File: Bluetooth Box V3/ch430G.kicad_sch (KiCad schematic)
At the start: 6 parts, among them U4 AMS1117-1.8, U8 AZ1117-3.3

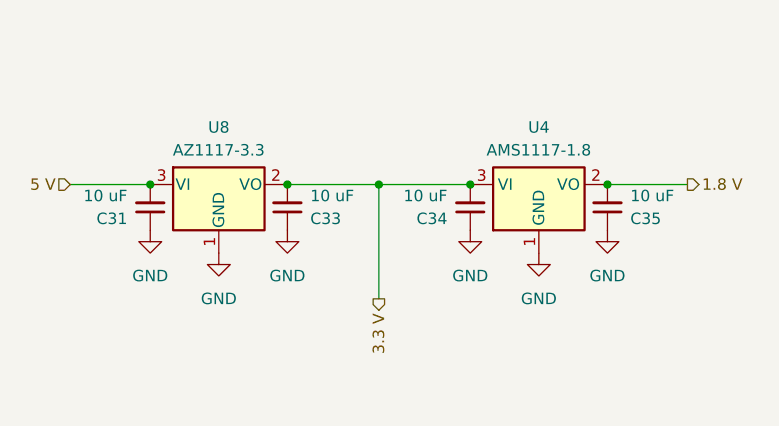
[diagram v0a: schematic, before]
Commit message: ESP32 Wechsel angefangen
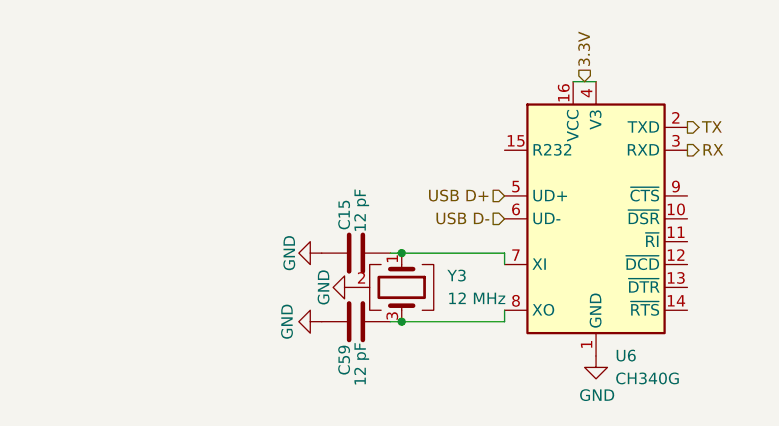
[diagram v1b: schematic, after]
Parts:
- removed C31, C33, C34, C35: 10 uF, Capacitor_SMD:C_0805_2012Metric, symbol Device:C_Small
- removed U4: AMS1117-1.8, Package_TO_SOT_SMD:SOT-223-3_TabPin2, symbol Regulator_Linear:AMS1117-1.8
- removed U8: AZ1117-3.3, Package_TO_SOT_SMD:TO-252-2, symbol Regulator_Linear:AZ1117-3.3
- added C15, C59: 12 pF, Capacitor_SMD:C_0805_2012Metric, symbol Device:C
- added U6: CH340G, Package_SO:SOIC-16_3.9x9.9mm_P1.27mm, symbol Interface_USB:CH340G
- added Y3: 12 MHz, Crystal:Crystal_SMD_3225-4Pin_3.2x2.5mm, symbol Device:Crystal_GND24
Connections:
- net GND: now also C15.1, C59.1, U6.1 (GND), Y3.2 (G), Y3.4 (G)
- new net: C15.2, U6.7 (XI), Y3.1
- new net: C59.2, U6.8 (XO), Y3.3
- new net 3.3V: U6.16 (VCC), U6.4 (V3)
- new net RX: U6.3 (RXD)
- new net TX: U6.2 (TXD)
- new net USB D+: U6.5 (UD+)
- new net USB D-: U6.6 (UD-)

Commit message: Idiotencheck #1
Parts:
- added C79: 100 nF, Capacitor_SMD:C_0805_2012Metric, symbol Device:C
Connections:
- net 3.3V: now also C79.2
- net GND: now also C79.1
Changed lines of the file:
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@@
 		(color 0 0 0 0)
 	)
+	(junction
+		(at 115.57 66.04)
+		(diameter 0)
+		(color 0 0 0 0)
+	)
+	(junction
+		(at 115.57 62.23)
+		(diameter 0)
+		(color 0 0 0 0)
+	)
+	(wire
+		(pts
+			(xy 115.57 66.04) (xy 116.84 66.04)
+		)
+		(stroke
+			(width 0)
+			(type default)
+		)
+	)
+	(wire
+		(pts
+			(xy 115.57 57.15) (xy 115.57 62.23)
+		)
+		(stroke
+			(width 0)
+			(type default)
+		)
+	)
 	(wire
 		(pts
@@
 	(wire
 		(pts
-			(xy 114.3 66.04) (xy 116.84 66.04)
+			(xy 114.3 66.04) (xy 115.57 66.04)
+		)
+		(stroke
+			(width 0)
+			(type default)
+		)
+	)
+	(wire
+		(pts
+			(xy 115.57 66.04) (xy 115.57 62.23)
 		)
 		(stroke
@@
 			(width 0)
 			(type default)
-		)
-	)
-	(hierarchical_label "3.3V"
-		(shape input)
-		(at 115.57 66.04 90)
-		(effects
-			(font
-				(size 1.27 1.27)
-			)
-			(justify left)
 		)
 	)
@@
 		)
 	)
+	(hierarchical_label "3.3V"
+		(shape input)
+		(at 115.57 57.15 90)
+		(effects
+			(font
+				(size 1.27 1.27)
+			)
+			(justify left)
+		)
+	)
+	(symbol
+		(lib_id "Device:C")
+		(at 119.38 62.23 270)
+		(mirror x)
+		(unit 1)
+		(body_style 1)
+		(exclude_from_sim no)
+		(in_bom yes)
+		(on_board yes)
+		(in_pos_files yes)
+		(dnp no)
+		(property "Reference" "C79"
+			(at 122.428 55.626 90)
+			(show_name no)
+			(do_not_autoplace no)
+			(effects
+				(font
+					(size 1.27 1.27)
+				)
+			)
+		)
+		(property "Value" "100 nF"
+			(at 122.428 58.166 90)
+			(show_name no)
+			(do_not_autoplace no)
+			(effects
+				(font
+					(size 1.27 1.27)
+				)
+			)
+		)
+		(property "Footprint" "Capacitor_SMD:C_0805_2012Metric"
+			(at 115.57 61.2648 0)
+			(hide yes)
+			(show_name no)
+			(do_not_autoplace no)
+			(effects
+				(font
+					(size 1.27 1.27)
+				)
+			)
+		)
+		(property "Datasheet" ""
+			(at 119.38 62.23 0)
+			(hide yes)
+			(show_name no)
+			(do_not_autoplace no)
+			(effects
+				(font
+					(size 1.27 1.27)
+				)
+			)
+		)
+		(property "Description" "Unpolarized capacitor"
+			(at 119.38 62.23 0)
+			(hide yes)
+			(show_name no)
+			(do_not_autoplace no)
+			(effects
+				(font
+					(size 1.27 1.27)
+				)
+			)
+		)
+		(property "LCSC Part #" "C49678"
+			(at 119.38 62.23 0)
+			(hide yes)
+			(show_name no)
+			(do_not_autoplace no)
+			(effects
+				(font
+					(size 1.27 1.27)
+				)
+			)
+		)
+		(pin "1"
+		)
+		(pin "2"
+		)
+		(instances
+			(project "Bluetooth Box V3"
+				(path "/c5f2915a-1379-46bf-9932-ae9df9d21574/1a2481a2-5ae9-408f-bbde-c21184b72b5d"
+					(reference "C79")
+					(unit 1)
+				)
+			)
+		)
+	)
+	(symbol
+		(lib_id "power:GND")
+		(at 123.19 62.23 90)
+		(unit 1)
+		(body_style 1)
+		(exclude_from_sim no)
+		(in_bom yes)
+		(on_board yes)
+		(in_pos_files yes)
+		(dnp no)
+		(property "Reference" "#PWR057"
+			(at 129.54 62.23 0)
+			(hide yes)
+			(show_name no)
+			(do_not_autoplace no)
+			(effects
+				(font
+					(size 1.27 1.27)
+				)
+			)
+		)
+		(property "Value" "GND"
+			(at 127.5842 62.103 0)
+			(show_name no)
+			(do_not_autoplace no)
+			(effects
+				(font
+					(size 1.27 1.27)
+				)
+			)
+		)
+		(property "Footprint" ""
+			(at 123.19 62.23 0)
+			(hide yes)
+			(show_name no)
+			(do_not_autoplace no)
+			(effects
+				(font
+					(size 1.27 1.27)
+				)
+			)
+		)
+		(property "Datasheet" ""
+			(at 123.19 62.23 0)
+			(hide yes)
+			(show_name no)
+			(do_not_autoplace no)
+			(effects
+				(font
+					(size 1.27 1.27)
+				)
+			)
+		)
+		(property "Description" ""
+			(at 123.19 62.23 0)
+			(show_name no)
+			(do_not_autoplace no)
+			(effects
+				(font
+					(size 1.27 1.27)
+				)
+			)
+		)
+		(pin "1"
+		)
+		(instances
+			(project "Bluetooth Box V3"
+				(path "/c5f2915a-1379-46bf-9932-ae9df9d21574/1a2481a2-5ae9-408f-bbde-c21184b72b5d"
+					(reference "#PWR057")
+					(unit 1)
+				)
+			)
+		)
+	)

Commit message: Grrr basti, grrr
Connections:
- net DTR: now reaches U6.13 (~{DTR})
- net RTS: now reaches U6.14 (~{RTS})
- no-connect marks 0 -> 5
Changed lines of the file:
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@@
 		(color 0 0 0 0)
+	)
+	(no_connect
+		(at 127 86.36)
+	)
+	(no_connect
+		(at 127 83.82)
+	)
+	(no_connect
+		(at 106.68 73.66)
+	)
+	(no_connect
+		(at 127 81.28)
+	)
+	(no_connect
+		(at 127 78.74)
 	)
 	(wire
@@
 		)
 	)
+	(hierarchical_label "DTR"
+		(shape output)
+		(at 127 88.9 0)
+		(effects
+			(font
+				(size 1.27 1.27)
+			)
+			(justify left)
+		)
+	)
 	(hierarchical_label "RX"
 		(shape output)
@@
 		(effects
 			(font
+				(size 1.27 1.27)
+			)
+			(justify left)
+		)
+	)
+	(hierarchical_label "RTS"
+		(shape output)
+		(at 127 91.44 0)
+		(effects
+			(font

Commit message: Try fixes
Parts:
- added C16: 1 uF, Capacitor_SMD:C_0603_1608Metric, symbol Device:C_Small
- added Q1: SS8050, Package_TO_SOT_SMD:SOT-23, symbol Simulation_SPICE:NPN
- added R16, R17, R30, R6: 10k Ohm, Resistor_SMD:R_0805_2012Metric, symbol Device:R_Small
- added SS8050: NPN, Package_TO_SOT_SMD:SOT-23, symbol Simulation_SPICE:NPN
- added SW2, SW3: KH-6X6X5H-STM, footprints:KH-6X6X5H-STM_SKE, symbol Personal:KH-6X6X5H-STM
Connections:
- net GND: now also C16.1
- net DTR: no longer names the net of U6.13 (~{DTR})
- net DTR: now also R6.1, SS8050.3 (E)
- net RTS: no longer names the net of U6.14 (~{RTS})
- net RTS: now also Q1.3 (E), R16.1
- new net: Q1.2 (B), R6.2
- new net: R17.1, SW2.A, SW2.B
- new net: R30.1, SW3.A, SW3.B
- new net: R16.2, SS8050.2 (B)
- new net +3V3: R17.2, R30.2
- new net EN: C16.2, Q1.1 (C), SW2.C, SW2.D
- new net IO0: SS8050.1 (C), SW3.C, SW3.D

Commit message: 4 layer
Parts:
- added C82: 100 nF, Capacitor_SMD:C_0805_2012Metric, symbol Device:C
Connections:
- net 3.3V: now also C82.1
- net GND: now also C82.2
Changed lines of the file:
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@@
+	)
+	(symbol
+		(lib_id "Device:C")
+		(at 111.76 62.23 270)
+		(mirror x)
+		(unit 1)
+		(body_style 1)
+		(exclude_from_sim no)
+		(in_bom yes)
+		(on_board yes)
+		(in_pos_files yes)
+		(dnp no)
+		(property "Reference" "C82"
+			(at 109.982 56.134 90)
+			(show_name no)
+			(do_not_autoplace no)
+			(effects
+				(font
+					(size 1.27 1.27)
+				)
+			)
+		)
+		(property "Value" "100 nF"
+			(at 109.982 58.674 90)
+			(show_name no)
+			(do_not_autoplace no)
+			(effects
+				(font
+					(size 1.27 1.27)
+				)
+			)
+		)
+		(property "Footprint" "Capacitor_SMD:C_0805_2012Metric"
+			(at 107.95 61.2648 0)
+			(hide yes)
+			(show_name no)
+			(do_not_autoplace no)
+			(effects
+				(font
+					(size 1.27 1.27)
+				)
+			)
+		)
+		(property "Datasheet" ""
+			(at 111.76 62.23 0)
+			(hide yes)
+			(show_name no)
+			(do_not_autoplace no)
+			(effects
+				(font
+					(size 1.27 1.27)
+				)
+			)
+		)
+		(property "Description" "Unpolarized capacitor"
+			(at 111.76 62.23 0)
+			(hide yes)
+			(show_name no)
+			(do_not_autoplace no)
+			(effects
+				(font
+					(size 1.27 1.27)
+				)
+			)
+		)
+		(property "LCSC Part #" "C49678"
+			(at 111.76 62.23 0)
+			(hide yes)
+			(show_name no)
+			(do_not_autoplace no)
+			(effects
+				(font
+					(size 1.27 1.27)
+				)
+			)
+		)
+		(pin "1"
+		)
+		(pin "2"
+		)
+		(instances
+			(project "Bluetooth Box V3"
+				(path "/c5f2915a-1379-46bf-9932-ae9df9d21574/1a2481a2-5ae9-408f-bbde-c21184b72b5d"
+					(reference "C82")
+					(unit 1)
+				)
+			)
+		)
 	)
 	(symbol
@@
 					(unit 1)
 				)
+			)
+		)
+	)
+	(symbol
+		(lib_id "power:GND")
+		(at 107.95 62.23 270)
+		(unit 1)
+		(body_style 1)
+		(exclude_from_sim no)
+		(in_bom yes)
+		(on_board yes)
+		(in_pos_files yes)
+		(dnp no)
+		(property "Reference" "#PWR0103"
+			(at 101.6 62.23 0)
+			(hide yes)
+			(show_name no)
+			(do_not_autoplace no)
+			(effects
+				(font
+					(size 1.27 1.27)
+				)
+			)
+		)
+		(property "Value" "GND"
+			(at 103.5558 62.357 0)
+			(show_name no)
+			(do_not_autoplace no)
+			(effects
+				(font
+					(size 1.27 1.27)
+				)
+			)
+		)
+		(property "Footprint" ""
+			(at 107.95 62.23 0)
+			(hide yes)
+			(show_name no)
+			(do_not_autoplace no)
+			(effects
+				(font
+					(size 1.27 1.27)
+				)
+			)
+		)
+		(property "Datasheet" ""
+			(at 107.95 62.23 0)
+			(hide yes)
+			(show_name no)
+			(do_not_autoplace no)
+			(effects
+				(font
+					(size 1.27 1.27)
+				)
+			)
+		)
+		(property "Description" ""
+			(at 107.95 62.23 0)
+			(show_name no)
+			(do_not_autoplace no)
+			(effects
+				(font
+					(size 1.27 1.27)
+				)
+			)
+		)
+		(pin "1"
+		)
+		(instances
+			(project "Bluetooth Box V3"
+				(path "/c5f2915a-1379-46bf-9932-ae9df9d21574/1a2481a2-5ae9-408f-bbde-c21184b72b5d"
+					(reference "#PWR0103")
+					(unit 1)
+				)

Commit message: jdfajjj
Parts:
- removed Q1: SS8050, Package_TO_SOT_SMD:SOT-23, symbol Simulation_SPICE:NPN
- removed SS8050: NPN, Package_TO_SOT_SMD:SOT-23, symbol Simulation_SPICE:NPN
- added Q2, Q3: SS8050, Package_TO_SOT_SMD:SOT-23, symbol Transistor_BJT:SS8050
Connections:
- net EN: now also Q2.3 (C)
- net IO0: now also Q3.3 (C)
- net at R6.1, U6.13 (~{DTR}): now also Q3.2 (E)
- net at R6.2: now also Q2.1 (B)
- net at R16.1, U6.14 (~{RTS}): now also Q2.2 (E)
- net at R16.2: now also Q3.1 (B)
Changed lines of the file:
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@@
+	)
+	(junction
+		(at 179.07 83.82)
+		(diameter 0)
+		(color 0 0 0 0)
 	)
 	(junction
@@
 	(junction
 		(at 198.12 60.96)
-		(diameter 0)
-		(color 0 0 0 0)
-	)
-	(junction
-		(at 179.07 83.82)
 		(diameter 0)
 		(color 0 0 0 0)
@@
 			)
 			(justify left)
+		)
+	)
+	(symbol
+		(lib_id "Transistor_BJT:SS8050")
+		(at 176.53 88.9 0)
+		(unit 1)
+		(body_style 1)
+		(exclude_from_sim no)
+		(in_bom yes)
+		(on_board yes)
+		(in_pos_files yes)
+		(dnp no)
+		(fields_autoplaced yes)
+		(property "Reference" "Q2"
+			(at 181.61 87.6299 0)
+			(show_name no)
+			(do_not_autoplace no)
+			(effects
+				(font
+					(size 1.27 1.27)
+				)
+				(justify left)
+			)
+		)
+		(property "Value" "SS8050"
+			(at 181.61 90.1699 0)
+			(show_name no)
+			(do_not_autoplace no)
+			(effects
+				(font
+					(size 1.27 1.27)
+				)
+				(justify left)
+			)
+		)
+		(property "Footprint" "Package_TO_SOT_SMD:SOT-23"
+			(at 181.61 96.266 0)
+			(hide yes)
+			(show_name no)
+			(do_not_autoplace no)
+			(effects
+				(font
+					(size 1.27 1.27)
+					(italic yes)
+				)
+				(justify left)
+			)
+		)
+		(property "Datasheet" "http://www.secosgmbh.com/datasheet/products/SSMPTransistor/SOT-23/SS8050.pdf"
+			(at 181.61 93.726 0)
+			(hide yes)
+			(show_name no)
+			(do_not_autoplace no)
+			(effects
+				(font
+					(size 1.27 1.27)
+				)
+				(justify left)
+			)
+		)
+		(property "Description" "General Purpose NPN Transistor, 1.5A Ic, 25V Vce, SOT-23"
+			(at 210.566 91.186 0)
+			(hide yes)
+			(show_name no)
+			(do_not_autoplace no)
+			(effects
+				(font
+					(size 1.27 1.27)
+				)
+			)
+		)
+		(property "Sim.Device" "NPN"
+			(at 176.53 88.9 0)
+			(hide yes)
+			(show_name no)
+			(do_not_autoplace no)
+			(effects
+				(font
+					(size 1.27 1.27)
+				)
+			)
+		)
+		(property "Sim.Pins" "1=B 2=E 3=C"
+			(at 176.53 88.9 0)
+			(hide yes)
+			(show_name no)
+			(do_not_autoplace no)
+			(effects
+				(font
+					(size 1.27 1.27)
+				)
+			)
+		)
+		(pin "3"
+		)
+		(pin "2"
+		)
+		(pin "1"
+		)
+		(instances
+			(project "Bluetooth Box V3"
+				(path "/c5f2915a-1379-46bf-9932-ae9df9d21574/1a2481a2-5ae9-408f-bbde-c21184b72b5d"
+					(reference "Q2")
+					(unit 1)
+				)
+			)
 		)
 	)
@@
 				(path "/c5f2915a-1379-46bf-9932-ae9df9d21574/1a2481a2-5ae9-408f-bbde-c21184b72b5d"
 					(reference "#PWR04")
+					(unit 1)
+				)
+			)
+		)
+	)
+	(symbol
+		(lib_id "Transistor_BJT:SS8050")
+		(at 176.53 104.14 0)
+		(mirror x)
+		(unit 1)
+		(body_style 1)
+		(exclude_from_sim no)
+		(in_bom yes)
+		(on_board yes)
+		(in_pos_files yes)
+		(dnp no)
+		(fields_autoplaced yes)
+		(property "Reference" "Q3"
+			(at 181.61 102.8699 0)
+			(show_name no)
+			(do_not_autoplace no)
+			(effects
+				(font
+					(size 1.27 1.27)
+				)
+				(justify left)
+			)
+		)
+		(property "Value" "SS8050"
+			(at 181.61 105.4099 0)
+			(show_name no)
+			(do_not_autoplace no)
+			(effects
+				(font
+					(size 1.27 1.27)
+				)
+				(justify left)
+			)
+		)
+		(property "Footprint" "Package_TO_SOT_SMD:SOT-23"
+			(at 181.61 96.774 0)
+			(hide yes)
+			(show_name no)
+			(do_not_autoplace no)
+			(effects
+				(font
+					(size 1.27 1.27)
+					(italic yes)
+				)
+				(justify left)
+			)
+		)
+		(property "Datasheet" "http://www.secosgmbh.com/datasheet/products/SSMPTransistor/SOT-23/SS8050.pdf"
+			(at 181.61 99.314 0)
+			(hide yes)
+			(show_name no)
+			(do_not_autoplace no)
+			(effects
+				(font
+					(size 1.27 1.27)
+				)
+				(justify left)
+			)
+		)
+		(property "Description" "General Purpose NPN Transistor, 1.5A Ic, 25V Vce, SOT-23"
+			(at 210.566 101.854 0)
+			(hide yes)
+			(show_name no)
+			(do_not_autoplace no)
+			(effects
+				(font
+					(size 1.27 1.27)
+				)
+			)
+		)
+		(property "Sim.Device" "NPN"
+			(at 176.53 104.14 0)
+			(hide yes)
+			(show_name no)
+			(do_not_autoplace no)
+			(effects
+				(font
+					(size 1.27 1.27)
+				)
+			)
+		)
+		(property "Sim.Pins" "1=B 2=E 3=C"
+			(at 176.53 104.14 0)
+			(hide yes)
+			(show_name no)
+			(do_not_autoplace no)
+			(effects
+				(font
+					(size 1.27 1.27)
+				)
+			)
+		)
+		(pin "3"
+		)
+		(pin "2"
+		)
+		(pin "1"
+		)
+		(instances
+			(project "Bluetooth Box V3"
+				(path "/c5f2915a-1379-46bf-9932-ae9df9d21574/1a2481a2-5ae9-408f-bbde-c21184b72b5d"
+					(reference "Q3")
 					(unit 1)
 				)
@@
 	)
 	(symbol
-		(lib_id "Simulation_SPICE:NPN")
-		(at 176.53 88.9 0)
-		(unit 1)
-		(body_style 1)
-		(exclude_from_sim no)
-		(in_bom yes)
-		(on_board yes)
-		(in_pos_files yes)
-		(dnp no)
-		(fields_autoplaced yes)
-		(property "Reference" "Q1"
-			(at 181.61 87.6299 0)
-			(show_name no)
-			(do_not_autoplace no)
-			(effects
-				(font
-					(size 1.27 1.27)
-				)
-				(justify left)
-			)
-		)
-		(property "Value" "SS8050"
-			(at 181.61 90.1699 0)
-			(show_name no)
-			(do_not_autoplace no)
-			(effects
-				(font
-					(size 1.27 1.27)
-				)
-				(justify left)
-			)
-		)
-		(property "Footprint" "Package_TO_SOT_SMD:SOT-23"
-			(at 240.03 88.9 0)
-			(hide yes)
-			(show_name no)
-			(do_not_autoplace no)
-			(effects
-				(font
-					(size 1.27 1.27)
-				)
-			)
-		)
-		(property "Datasheet" "https://ngspice.sourceforge.io/docs/ngspice-html-manual/manual.xhtml#cha_BJTs"
-			(at 240.03 88.9 0)
-			(hide yes)
-			(show_name no)
-			(do_not_autoplace no)
-			(effects
-				(font
-					(size 1.27 1.27)
-				)
-			)
-		)
-		(property "Description" "Bipolar transistor symbol for simulation only, substrate tied to the emitter"
-			(at 176.53 88.9 0)
-			(hide yes)
-			(show_name no)
-			(do_not_autoplace no)
-			(effects
-				(font
-					(size 1.27 1.27)
-				)
-			)
-		)
-		(property "Sim.Device" "NPN"
-			(at 176.53 88.9 0)
-			(hide yes)
-			(show_name no)
-			(do_not_autoplace no)
-			(effects
-				(font
-					(size 1.27 1.27)
-				)
-			)
-		)
-		(property "Sim.Type" "GUMMELPOON"
-			(at 176.53 88.9 0)
-			(hide yes)
-			(show_name no)
-			(do_not_autoplace no)
-			(effects
-				(font
-					(size 1.27 1.27)
-				)
-			)
-		)
-		(property "Sim.Pins" "1=C 2=B 3=E"
-			(at 176.53 88.9 0)
-			(hide yes)
-			(show_name no)
-			(do_not_autoplace no)
-			(effects
-				(font
-					(size 1.27 1.27)
-				)
-			)
-		)
-		(pin "2"
-		)
-		(pin "3"
-		)
-		(pin "1"
-		)
-		(instances
-			(project "Bluetooth Box V3"
-				(path "/c5f2915a-1379-46bf-9932-ae9df9d21574/1a2481a2-5ae9-408f-bbde-c21184b72b5d"
-					(reference "Q1")
-					(unit 1)
-				)
-			)
-		)
-	)
-	(symbol
 		(lib_id "Personal:KH-6X6X5H-STM")
 		(at 198.12 140.97 180)
@@
 					(unit 1)
 				)
-			)
-		)
-	)
-	(symbol
-		(lib_id "Simulation_SPICE:NPN")
-		(at 176.53 104.14 0)
-		(mirror x)
-		(unit 1)
-		(body_style 1)
-		(exclude_from_sim no)
-		(in_bom yes)
-		(on_board yes)
-		(in_pos_files yes)
-		(dnp no)
-		(fields_autoplaced yes)
-		(property "Reference" "SS8050"
-			(at 181.61 105.4101 0)
-			(show_name no)
-			(do_not_autoplace no)
-			(effects
-				(font
-					(size 1.27 1.27)
-				)
-				(justify left)
-			)
-		)
-		(property "Value" "NPN"
-			(at 181.61 102.8701 0)
-			(show_name no)
-			(do_not_autoplace no)
-			(effects
-				(font
-					(size 1.27 1.27)
-				)
-				(justify left)
-			)
-		)
-		(property "Footprint" "Package_TO_SOT_SMD:SOT-23"
-			(at 240.03 104.14 0)
-			(hide yes)
-			(show_name no)
-			(do_not_autoplace no)
-			(effects
-				(font
-					(size 1.27 1.27)
-				)
-			)
-		)
-		(property "Datasheet" "https://ngspice.sourceforge.io/docs/ngspice-html-manual/manual.xhtml#cha_BJTs"
-			(at 240.03 104.14 0)
-			(hide yes)
-			(show_name no)
-			(do_not_autoplace no)
-			(effects
-				(font
-					(size 1.27 1.27)
-				)
-			)
-		)
-		(property "Description" "Bipolar transistor symbol for simulation only, substrate tied to the emitter"
-			(at 176.53 104.14 0)
-			(hide yes)
-			(show_name no)
-			(do_not_autoplace no)
-			(effects
-				(font
-					(size 1.27 1.27)
-				)
-			)
-		)
-		(property "Sim.Device" "NPN"
-			(at 176.53 104.14 0)
-			(hide yes)
-			(show_name no)
-			(do_not_autoplace no)
-			(effects
-				(font
-					(size 1.27 1.27)
-				)
-			)
-		)
-		(property "Sim.Type" "GUMMELPOON"
-			(at 176.53 104.14 0)
-			(hide yes)
-			(show_name no)
-			(do_not_autoplace no)
-			(effects
-				(font
-					(size 1.27 1.27)
-				)
-			)
-		)
-		(property "Sim.Pins" "1=C 2=B 3=E"
-			(at 176.53 104.14 0)
-			(hide yes)
-			(show_name no)
-			(do_not_autoplace no)
-			(effects
-				(font
-					(size 1.27 1.27)
-				)
-			)
-		)
-		(pin "2"
-		)
-		(pin "3"
-		)
-		(pin "1"
-		)
-		(instances
-			(project "Bluetooth Box V3"
-				(path "/c5f2915a-1379-46bf-9932-ae9df9d21574/1a2481a2-5ae9-408f-bbde-c21184b72b5d"
-					(reference "SS8050")
-					(unit 1)
-				)
